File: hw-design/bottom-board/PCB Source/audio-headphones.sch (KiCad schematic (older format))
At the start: 20 parts, among them Q17 J110, Q8 J110, U14 LM4811

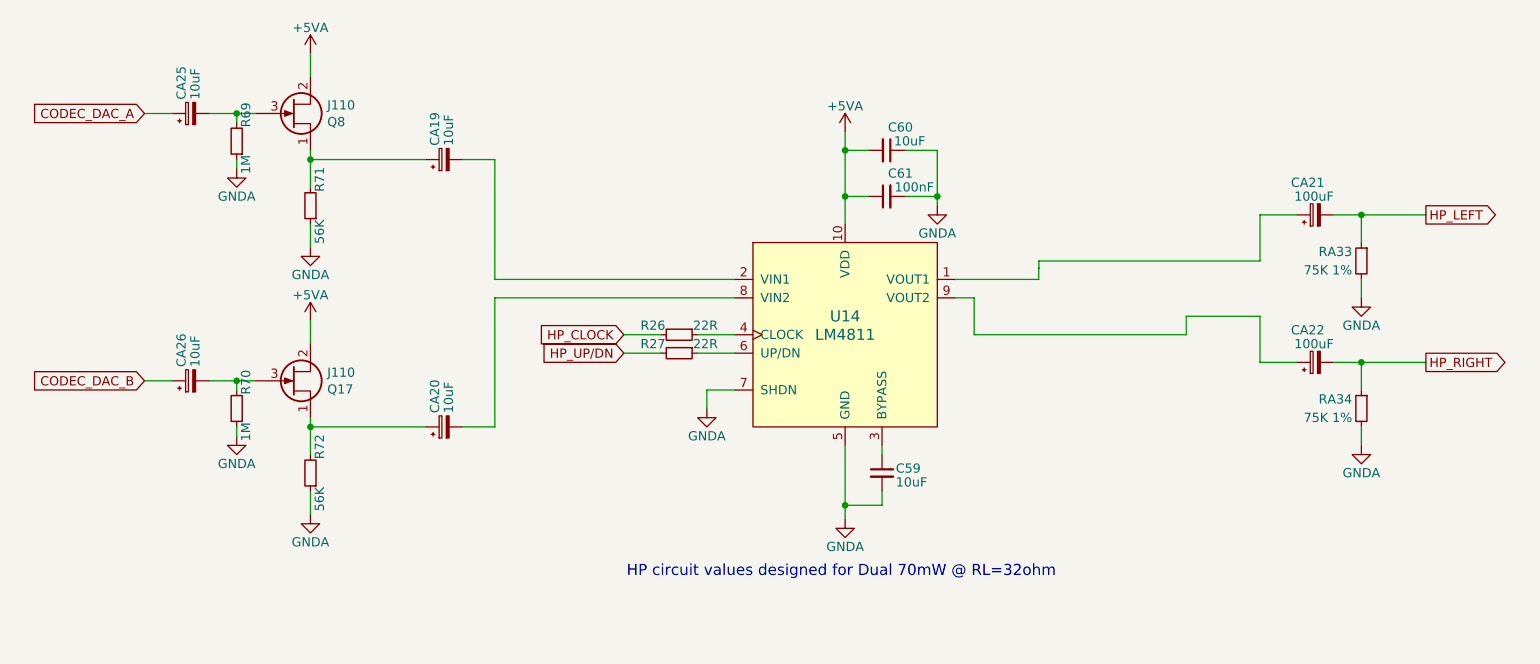
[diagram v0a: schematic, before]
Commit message: redo headphone output
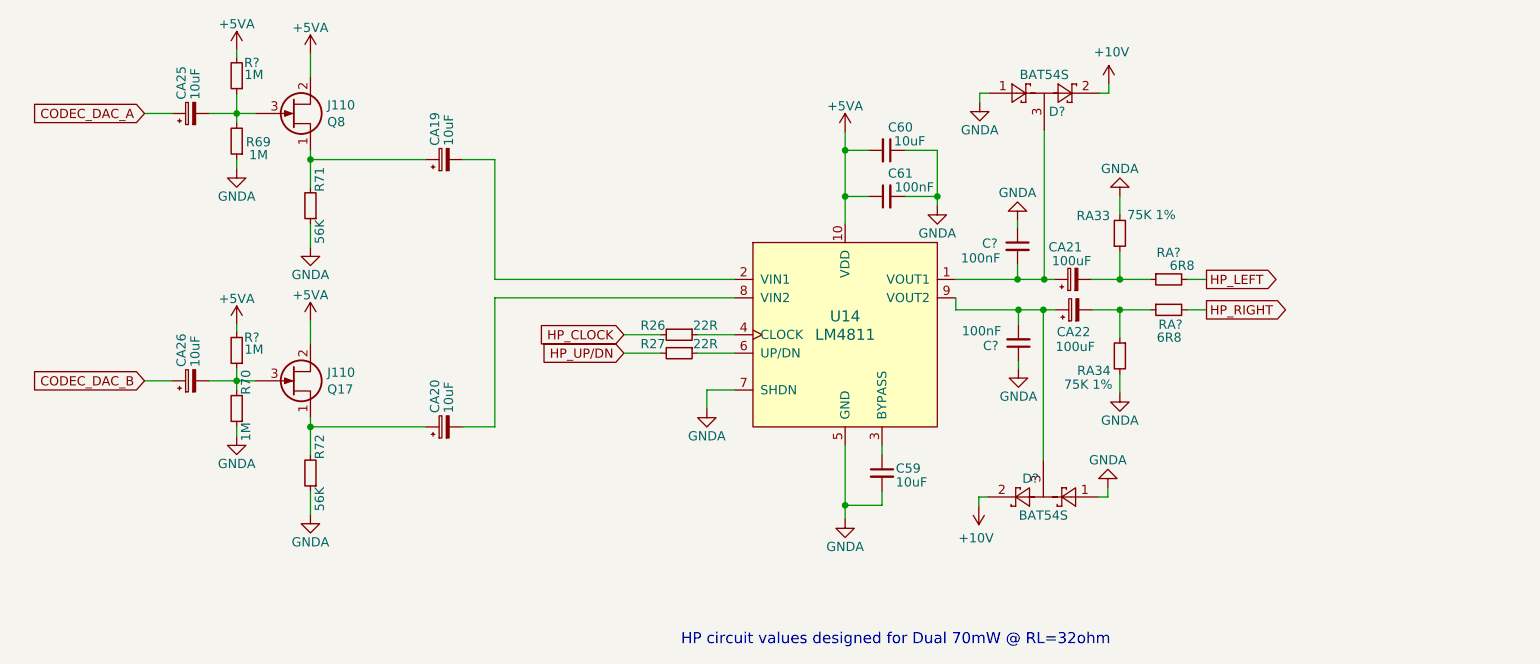
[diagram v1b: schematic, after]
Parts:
- added C? (x2): 100nF, Capacitor_SMD:C_0603_1608Metric, symbol bottom-board-rescue:C_Small-Device
- added D? (x2): BAT54S, Package_TO_SOT_SMD:SOT-23, symbol bottom-board-rescue:BAT54S-Diode
- added R? (x2): 1M, Resistor_SMD:R_0603_1608Metric, symbol bottom-board-rescue:R_Small-Device
- added RA? (x2): 6R8, Resistor_SMD:R_0603_1608Metric, symbol bottom-board-rescue:R_Small-Device
- Q17, Q8: MPN PMBFJ110,215 -> MMBFJ110
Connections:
- net +5VA: now also R?.2, R?.2
- net GNDA: now also C?.1, C?.1, D?.1, D?.1
- net HP_LEFT: now also RA?.2; no longer CA21.2, RA33.1
- net HP_RIGHT: now also RA?.2; no longer CA22.2, RA34.1
- net at CA21.1, U14.1 (VOUT1): now also C?.2, D?.3
- net at CA22.1, U14.9 (VOUT2): now also C?.2, D?.3
- net at CA26.2, Q17.3 (G), R70.2: now also R?.1
- net at CA25.2, Q8.3 (G), R69.2: now also R?.1
- new net: CA21.2, RA33.1, RA?.1
- new net: CA22.2, RA34.1, RA?.1
- new net +10V: D?.2, D?.2
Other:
- moved on the sheet: CA21, CA22, RA33, RA34

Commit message: place new power curcuit on the PCB
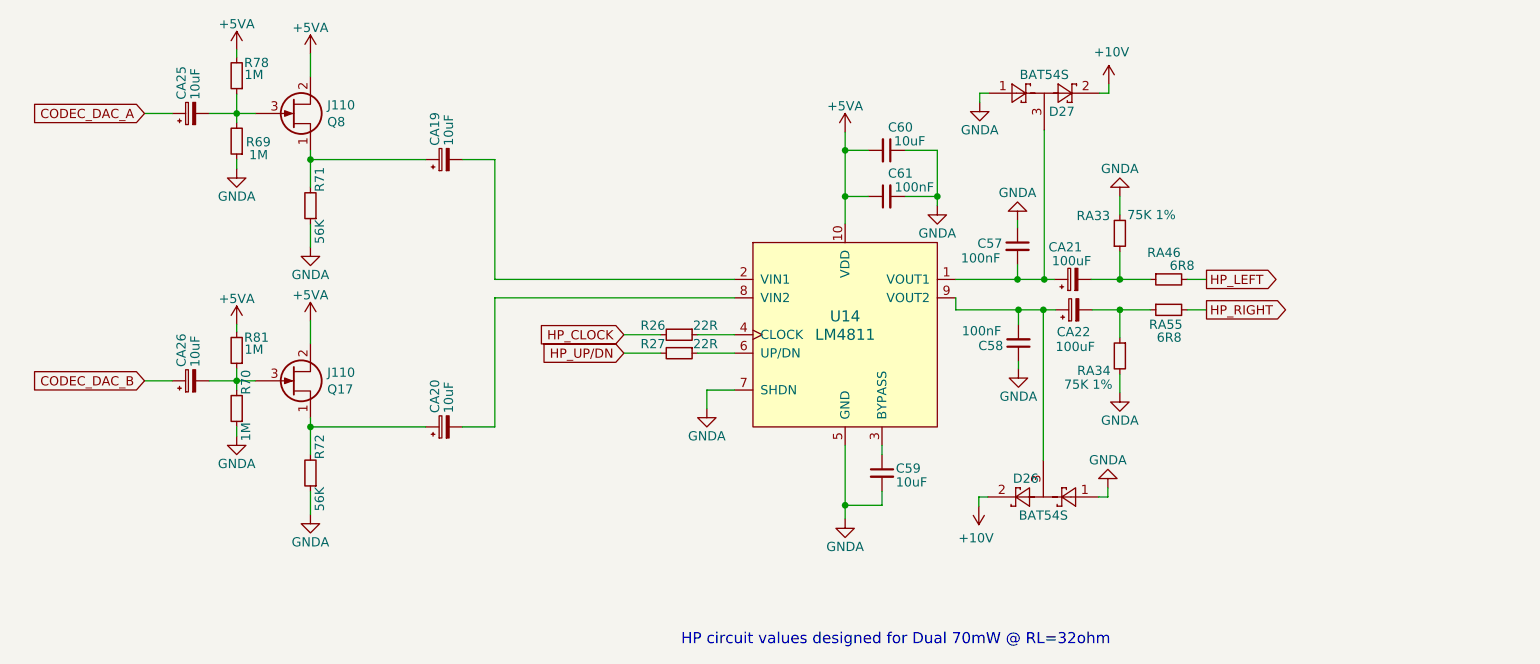
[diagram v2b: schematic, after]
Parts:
- gave numbers to parts that had none: 8
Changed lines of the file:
@@
 F 1 "J110" H 3341 3255 50  0000 L CNN
 F 2 "Package_TO_SOT_SMD:SOT-23" H 3350 3400 50  0001 C CNN
-F 3 "https://www.nxp.com/docs/en/data-sheet/PMBFJ108_109_110.pdf" H 3150 3300 50  0001 C CNN
+F 3 "" H 3150 3300 50  0001 C CNN
 F 4 "MMBFJ110" H 3150 3300 50  0001 C CNN "MPN"
 	1    3150 3300
@@
 F 1 "J110" H 3341 1805 50  0000 L CNN
 F 2 "Package_TO_SOT_SMD:SOT-23" H 3350 1950 50  0001 C CNN
-F 3 "https://www.nxp.com/docs/en/data-sheet/PMBFJ108_109_110.pdf" H 3150 1850 50  0001 C CNN
+F 3 "" H 3150 1850 50  0001 C CNN
 F 4 "MMBFJ110" H 3150 1850 50  0001 C CNN "MPN"
 	1    3150 1850
@@
 P 2850 1645
 AR Path="/54F72B97/624FE43D" Ref="R?"  Part="1"
-AR Path="/54F72F64/624FE43D" Ref="R?"  Part="1"
-F 0 "R?" H 2810 1575 50  0000 R CNN
+AR Path="/54F72F64/624FE43D" Ref="R78"  Part="1"
+F 0 "R78" H 2810 1575 50  0000 R CNN
 F 1 "1M" H 2705 1640 50  0000 L CNN
 F 2 "Resistor_SMD:R_0603_1608Metric" H 2850 1645 60  0001 C CNN
@@
 $EndComp
 $Comp
-L bottom-board-rescue:+5VA-power #PWR?
+L bottom-board-rescue:+5VA-power #PWR0298
 U 1 1 624FF279
 P 2850 1505
-F 0 "#PWR?" H 2850 1355 50  0001 C CNN
+F 0 "#PWR0298" H 2850 1355 50  0001 C CNN
 F 1 "+5VA" H 2850 1645 50  0000 C CNN
 F 2 "" H 2850 1505 50  0001 C CNN
@@
 P 2850 3135
 AR Path="/54F72B97/6250DA2F" Ref="R?"  Part="1"
-AR Path="/54F72F64/6250DA2F" Ref="R?"  Part="1"
-F 0 "R?" H 2810 3065 50  0000 R CNN
+AR Path="/54F72F64/6250DA2F" Ref="R81"  Part="1"
+F 0 "R81" H 2810 3065 50  0000 R CNN
 F 1 "1M" H 2705 3130 50  0000 L CNN
 F 2 "Resistor_SMD:R_0603_1608Metric" H 2850 3135 60  0001 C CNN
@@
 $EndComp
 $Comp
-L bottom-board-rescue:+5VA-power #PWR?
+L bottom-board-rescue:+5VA-power #PWR0299
 U 1 1 6250DA35
 P 2850 2995
-F 0 "#PWR?" H 2850 2845 50  0001 C CNN
+F 0 "#PWR0299" H 2850 2845 50  0001 C CNN
 F 1 "+5VA" H 2850 3135 50  0000 C CNN
 F 2 "" H 2850 2995 50  0001 C CNN
@@
 AR Path="/54F72B97/62533F5B" Ref="D?"  Part="1"
 AR Path="/54F72C8D/62533F5B" Ref="D?"  Part="1"
-AR Path="/54F72F64/62533F5B" Ref="D?"  Part="1"
-F 0 "D?" H 7255 1640 50  0000 L CNN
+AR Path="/54F72F64/62533F5B" Ref="D27"  Part="1"
+F 0 "D27" H 7255 1640 50  0000 L CNN
 F 1 "BAT54S" H 7230 1840 50  0000 C CNN
 F 2 "Package_TO_SOT_SMD:SOT-23" H 7305 1865 50  0001 L CNN
@@
 P 6880 1790
 AR Path="/54F72C8D/62533F62" Ref="#PWR?"  Part="1"
-AR Path="/54F72F64/62533F62" Ref="#PWR?"  Part="1"
-F 0 "#PWR?" H 6880 1540 50  0001 C CNN
+AR Path="/54F72F64/62533F62" Ref="#PWR0300"  Part="1"
+F 0 "#PWR0300" H 6880 1540 50  0001 C CNN
 F 1 "GNDA" H 6880 1640 50  0000 C CNN
 F 2 "" H 6880 1790 60  0000 C CNN
@@
 P 7580 1690
 AR Path="/54F72C8D/62533F6A" Ref="#PWR?"  Part="1"
-AR Path="/54F72F64/62533F6A" Ref="#PWR?"  Part="1"
-F 0 "#PWR?" H 7580 1540 50  0001 C CNN
+AR Path="/54F72F64/62533F6A" Ref="#PWR0301"  Part="1"
+F 0 "#PWR0301" H 7580 1540 50  0001 C CNN
 F 1 "+10V" H 7595 1863 50  0000 C CNN
 F 2 "" H 7580 1690 50  0001 C CNN
@@
 AR Path="/54F72C8D/625369F6" Ref="C?"  Part="1"
 AR Path="/54F72CD0/625369F6" Ref="C?"  Part="1"
-AR Path="/54F72F64/625369F6" Ref="C?"  Part="1"
-F 0 "C?" H 6935 2585 50  0000 C CNN
+AR Path="/54F72F64/625369F6" Ref="C57"  Part="1"
+F 0 "C57" H 6935 2585 50  0000 C CNN
 F 1 "100nF" H 6885 2505 50  0000 C CNN
 F 2 "Capacitor_SMD:C_0603_1608Metric" H 7085 2570 60  0001 C CNN
@@
 $EndComp
 $Comp
-L bottom-board-rescue:GNDA-power #PWR?
+L bottom-board-rescue:GNDA-power #PWR0302
 U 1 1 6253DE76
 P 7085 2430
-F 0 "#PWR?" H 7085 2180 50  0001 C CNN
+F 0 "#PWR0302" H 7085 2180 50  0001 C CNN
 F 1 "GNDA" H 7085 2280 50  0000 C CNN
 F 2 "" H 7085 2430 60  0000 C CNN
@@
 AR Path="/54F72C8D/6254FB96" Ref="C?"  Part="1"
 AR Path="/54F72CD0/6254FB96" Ref="C?"  Part="1"
-AR Path="/54F72F64/6254FB96" Ref="C?"  Part="1"
-F 0 "C?" H 6940 3110 50  0000 C CNN
+AR Path="/54F72F64/6254FB96" Ref="C58"  Part="1"
+F 0 "C58" H 6940 3110 50  0000 C CNN
 F 1 "100nF" H 6890 3030 50  0000 C CNN
 F 2 "Capacitor_SMD:C_0603_1608Metric" H 7090 3095 60  0001 C CNN
@@
 $EndComp
 $Comp
-L bottom-board-rescue:GNDA-power #PWR?
+L bottom-board-rescue:GNDA-power #PWR0303
 U 1 1 6254FB9C
 P 7090 3235
-F 0 "#PWR?" H 7090 2985 50  0001 C CNN
+F 0 "#PWR0303" H 7090 2985 50  0001 C CNN
 F 1 "GNDA" H 7090 3085 50  0000 C CNN
 F 2 "" H 7090 3235 60  0000 C CNN
@@
 P 7905 2750
 AR Path="/54F72CD0/62578939" Ref="RA?"  Part="1"
-AR Path="/54F72F64/62578939" Ref="RA?"  Part="1"
-F 0 "RA?" V 7760 2685 50  0000 L CNN
+AR Path="/54F72F64/62578939" Ref="RA46"  Part="1"
+F 0 "RA46" V 7760 2685 50  0000 L CNN
 F 1 "6R8" V 7830 2610 50  0000 L CNN
 F 2 "Resistor_SMD:R_0603_1608Metric" H 7905 2750 60  0001 C CNN
@@
 P 7905 2915
 AR Path="/54F72CD0/62598A2E" Ref="RA?"  Part="1"
-AR Path="/54F72F64/62598A2E" Ref="RA?"  Part="1"
-F 0 "RA?" V 7985 2840 50  0000 L CNN
+AR Path="/54F72F64/62598A2E" Ref="RA55"  Part="1"
+F 0 "RA55" V 7985 2840 50  0000 L CNN
 F 1 "6R8" V 8055 2845 50  0000 L CNN
 F 2 "Resistor_SMD:R_0603_1608Metric" H 7905 2915 60  0001 C CNN
@@
 AR Path="/54F72B97/625BB3AF" Ref="D?"  Part="1"
 AR Path="/54F72C8D/625BB3AF" Ref="D?"  Part="1"
-AR Path="/54F72F64/625BB3AF" Ref="D?"  Part="1"
-F 0 "D?" H 7250 3830 50  0000 L CNN
+AR Path="/54F72F64/625BB3AF" Ref="D26"  Part="1"
+F 0 "D26" H 7250 3830 50  0000 L CNN
 F 1 "BAT54S" H 7225 4030 50  0000 C CNN
 F 2 "Package_TO_SOT_SMD:SOT-23" H 7300 4055 50  0001 L CNN
@@
 P 7575 3880
 AR Path="/54F72C8D/625BB3B6" Ref="#PWR?"  Part="1"
-AR Path="/54F72F64/625BB3B6" Ref="#PWR?"  Part="1"
-F 0 "#PWR?" H 7575 3630 50  0001 C CNN
+AR Path="/54F72F64/625BB3B6" Ref="#PWR0304"  Part="1"
+F 0 "#PWR0304" H 7575 3630 50  0001 C CNN
 F 1 "GNDA" H 7575 3730 50  0000 C CNN
 F 2 "" H 7575 3880 60  0000 C CNN
@@
 P 6875 3980
 AR Path="/54F72C8D/625BB3BE" Ref="#PWR?"  Part="1"
-AR Path="/54F72F64/625BB3BE" Ref="#PWR?"  Part="1"
-F 0 "#PWR?" H 6875 3830 50  0001 C CNN
+AR Path="/54F72F64/625BB3BE" Ref="#PWR0305"  Part="1"
+F 0 "#PWR0305" H 6875 3830 50  0001 C CNN
 F 1 "+10V" H 6890 4153 50  0000 C CNN
 F 2 "" H 6875 3980 50  0001 C CNN

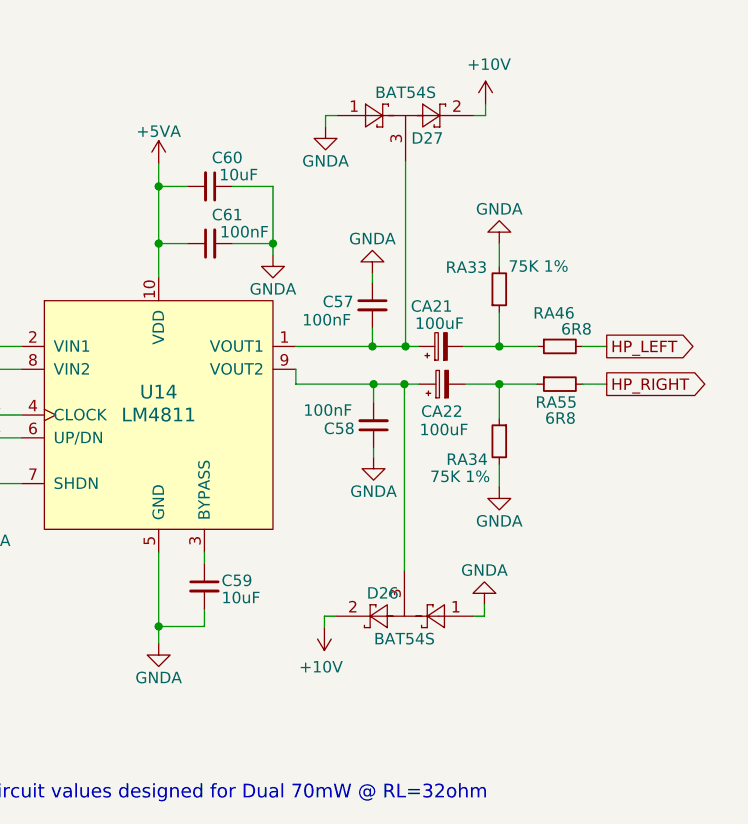
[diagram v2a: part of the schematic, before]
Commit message: first half of star ground
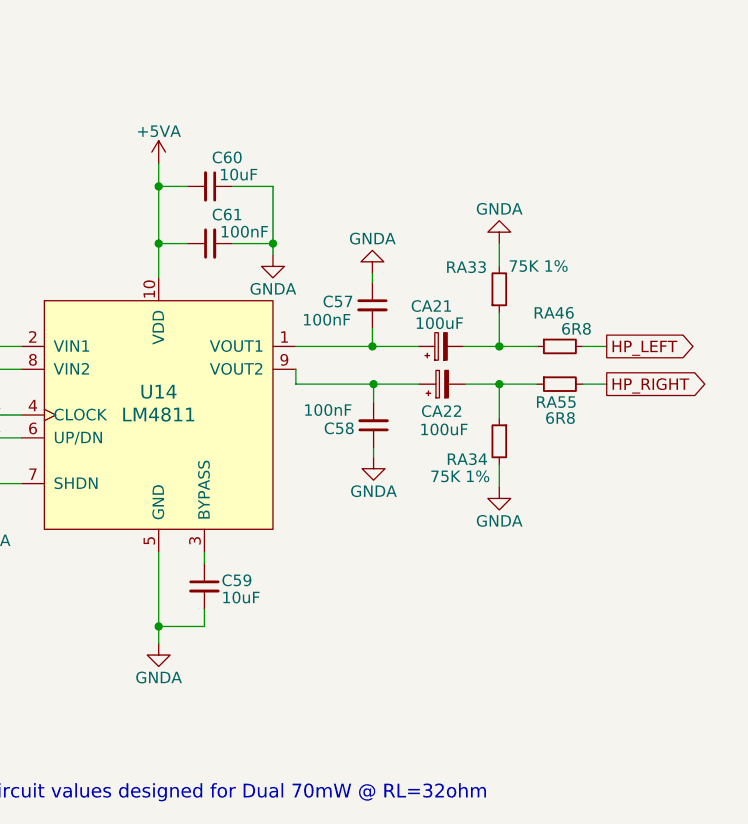
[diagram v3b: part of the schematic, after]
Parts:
- removed D26, D27: BAT54S, Package_TO_SOT_SMD:SOT-23, symbol bottom-board-rescue:BAT54S-Diode
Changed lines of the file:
@@
 $EndDescr
-$Comp
-L bottom-board-rescue:LM4811-local-components U14
-U 1 1 550D498D
-P 6150 3050
-F 0 "U14" H 6150 3150 60  0000 C CNN
-F 1 "LM4811" H 6150 3050 60  0000 C CNN
-F 2 "Package_SO:MSOP-10_3x3mm_P0.5mm" H 6150 3050 60  0001 C CNN
-F 3 "http://www.ti.com/lit/ds/symlink/lm4811.pdf" H 6150 3050 60  0001 C CNN
-F 4 "LM4811MM/NOPB" H 800 1050 50  0001 C CNN "MPN"
-	1    6150 3050
-	1    0    0    -1
-$EndComp
 $Comp
 L bottom-board-rescue:GNDA-power #PWR0150
@@
 Text GLabel 8110 2750 2    50   Output ~ 0
 HP_LEFT
-Wire Wire Line
-	7085 2750 7230 2750
 $Comp
 L bottom-board-rescue:CP_Small-Device CA?
@@
 Wire Wire Line
 	2850 3235 2850 3300
-Wire Wire Line
-	7580 1740 7530 1740
-$Comp
-L bottom-board-rescue:BAT54S-Diode D?
-U 1 1 62533F5B
-P 7230 1740
-AR Path="/54F72B97/62533F5B" Ref="D?"  Part="1"
-AR Path="/54F72C8D/62533F5B" Ref="D?"  Part="1"
-AR Path="/54F72F64/62533F5B" Ref="D27"  Part="1"
-F 0 "D27" H 7255 1640 50  0000 L CNN
-F 1 "BAT54S" H 7230 1840 50  0000 C CNN
-F 2 "Package_TO_SOT_SMD:SOT-23" H 7305 1865 50  0001 L CNN
-F 3 "https://www.diodes.com/assets/Datasheets/ds11005.pdf" H 7110 1740 50  0001 C CNN
-F 4 "BAT54SFILM" V 7230 1740 50  0001 C CNN "MPN"
-	1    7230 1740
-	1    0    0    -1
-$EndComp
-Wire Wire Line
-	7580 1740 7580 1690
-$Comp
-L bottom-board-rescue:GNDA-power #PWR?
-U 1 1 62533F62
-P 6880 1790
-AR Path="/54F72C8D/62533F62" Ref="#PWR?"  Part="1"
-AR Path="/54F72F64/62533F62" Ref="#PWR0300"  Part="1"
-F 0 "#PWR0300" H 6880 1540 50  0001 C CNN
-F 1 "GNDA" H 6880 1640 50  0000 C CNN
-F 2 "" H 6880 1790 60  0000 C CNN
-F 3 "" H 6880 1790 60  0000 C CNN
-	1    6880 1790
-	1    0    0    -1
-$EndComp
-Wire Wire Line
-	6880 1790 6880 1740
-Wire Wire Line
-	6880 1740 6930 1740
-$Comp
-L power:+10V #PWR?
-U 1 1 62533F6A
-P 7580 1690
-AR Path="/54F72C8D/62533F6A" Ref="#PWR?"  Part="1"
-AR Path="/54F72F64/62533F6A" Ref="#PWR0301"  Part="1"
-F 0 "#PWR0301" H 7580 1540 50  0001 C CNN
-F 1 "+10V" H 7595 1863 50  0000 C CNN
-F 2 "" H 7580 1690 50  0001 C CNN
-F 3 "" H 7580 1690 50  0001 C CNN
-	1    7580 1690
-	1    0    0    -1
-$EndComp
 $Comp
 L bottom-board-rescue:C_Small-Device C?
@@
 	7085 2430 7085 2470
 Connection ~ 7085 2750
-Wire Wire Line
-	7090 2915 7225 2915
 $Comp
 L bottom-board-rescue:C_Small-Device C?
@@
 	8110 2915 8005 2915
 Wire Wire Line
-	7230 1940 7230 2750
-Connection ~ 7230 2750
-Wire Wire Line
-	7230 2750 7285 2750
-Wire Wire Line
-	6875 3930 6925 3930
-$Comp
-L bottom-board-rescue:BAT54S-Diode D?
-U 1 1 625BB3AF
-P 7225 3930
-AR Path="/54F72B97/625BB3AF" Ref="D?"  Part="1"
-AR Path="/54F72C8D/625BB3AF" Ref="D?"  Part="1"
-AR Path="/54F72F64/625BB3AF" Ref="D26"  Part="1"
-F 0 "D26" H 7250 3830 50  0000 L CNN
-F 1 "BAT54S" H 7225 4030 50  0000 C CNN
-F 2 "Package_TO_SOT_SMD:SOT-23" H 7300 4055 50  0001 L CNN
-F 3 "https://www.diodes.com/assets/Datasheets/ds11005.pdf" H 7105 3930 50  0001 C CNN
-F 4 "BAT54SFILM" V 7225 3930 50  0001 C CNN "MPN"
-	1    7225 3930
-	-1   0    0    1
-$EndComp
-Wire Wire Line
-	6875 3930 6875 3980
-$Comp
-L bottom-board-rescue:GNDA-power #PWR?
-U 1 1 625BB3B6
-P 7575 3880
-AR Path="/54F72C8D/625BB3B6" Ref="#PWR?"  Part="1"
-AR Path="/54F72F64/625BB3B6" Ref="#PWR0304"  Part="1"
-F 0 "#PWR0304" H 7575 3630 50  0001 C CNN
-F 1 "GNDA" H 7575 3730 50  0000 C CNN
-F 2 "" H 7575 3880 60  0000 C CNN
-F 3 "" H 7575 3880 60  0000 C CNN
-	1    7575 3880
-	-1   0    0    1
-$EndComp
-Wire Wire Line
-	7575 3880 7575 3930
-Wire Wire Line
-	7575 3930 7525 3930
-$Comp
-L power:+10V #PWR?
-U 1 1 625BB3BE
-P 6875 3980
-AR Path="/54F72C8D/625BB3BE" Ref="#PWR?"  Part="1"
-AR Path="/54F72F64/625BB3BE" Ref="#PWR0305"  Part="1"
-F 0 "#PWR0305" H 6875 3830 50  0001 C CNN
-F 1 "+10V" H 6890 4153 50  0000 C CNN
-F 2 "" H 6875 3980 50  0001 C CNN
-F 3 "" H 6875 3980 50  0001 C CNN
-	1    6875 3980
-	-1   0    0    1
-$EndComp
-Wire Wire Line
-	7225 2915 7225 3730
-Connection ~ 7225 2915
-Wire Wire Line
-	7225 2915 7290 2915
+	7085 2750 7285 2750
+$Comp
+L bottom-board-rescue:LM4811-local-components U14
+U 1 1 550D498D
+P 6150 3050
+F 0 "U14" H 6150 3150 60  0000 C CNN
+F 1 "LM4811" H 6150 3050 60  0000 C CNN
+F 2 "Package_SO:MSOP-10_3x3mm_P0.5mm" H 6150 3050 60  0001 C CNN
+F 3 "http://www.ti.com/lit/ds/symlink/lm4811.pdf" H 6150 3050 60  0001 C CNN
+F 4 "LM4811MM/NOPB" H 800 1050 50  0001 C CNN "MPN"
+	1    6150 3050
+	1    0    0    -1
+$EndComp
+Wire Wire Line
+	7090 2915 7290 2915
 $EndSCHEMATC
